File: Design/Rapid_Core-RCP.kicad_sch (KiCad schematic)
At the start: 1 part, among them U1 STM32F446RETx

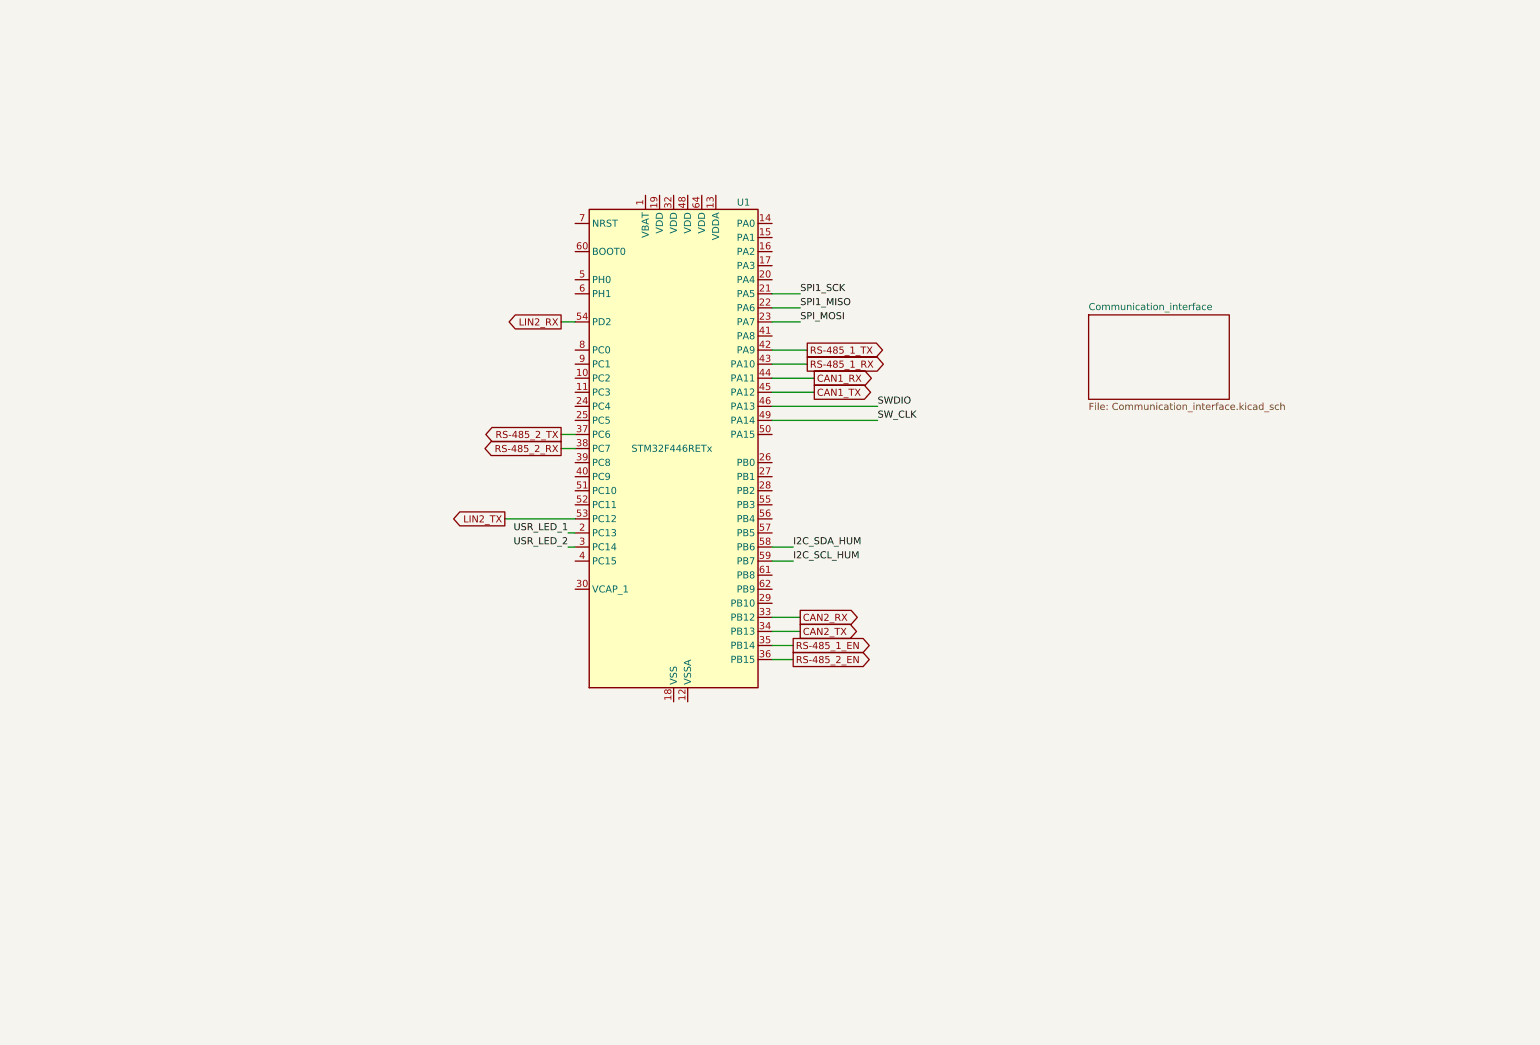
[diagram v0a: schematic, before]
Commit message: Added Comps in Communication.sch
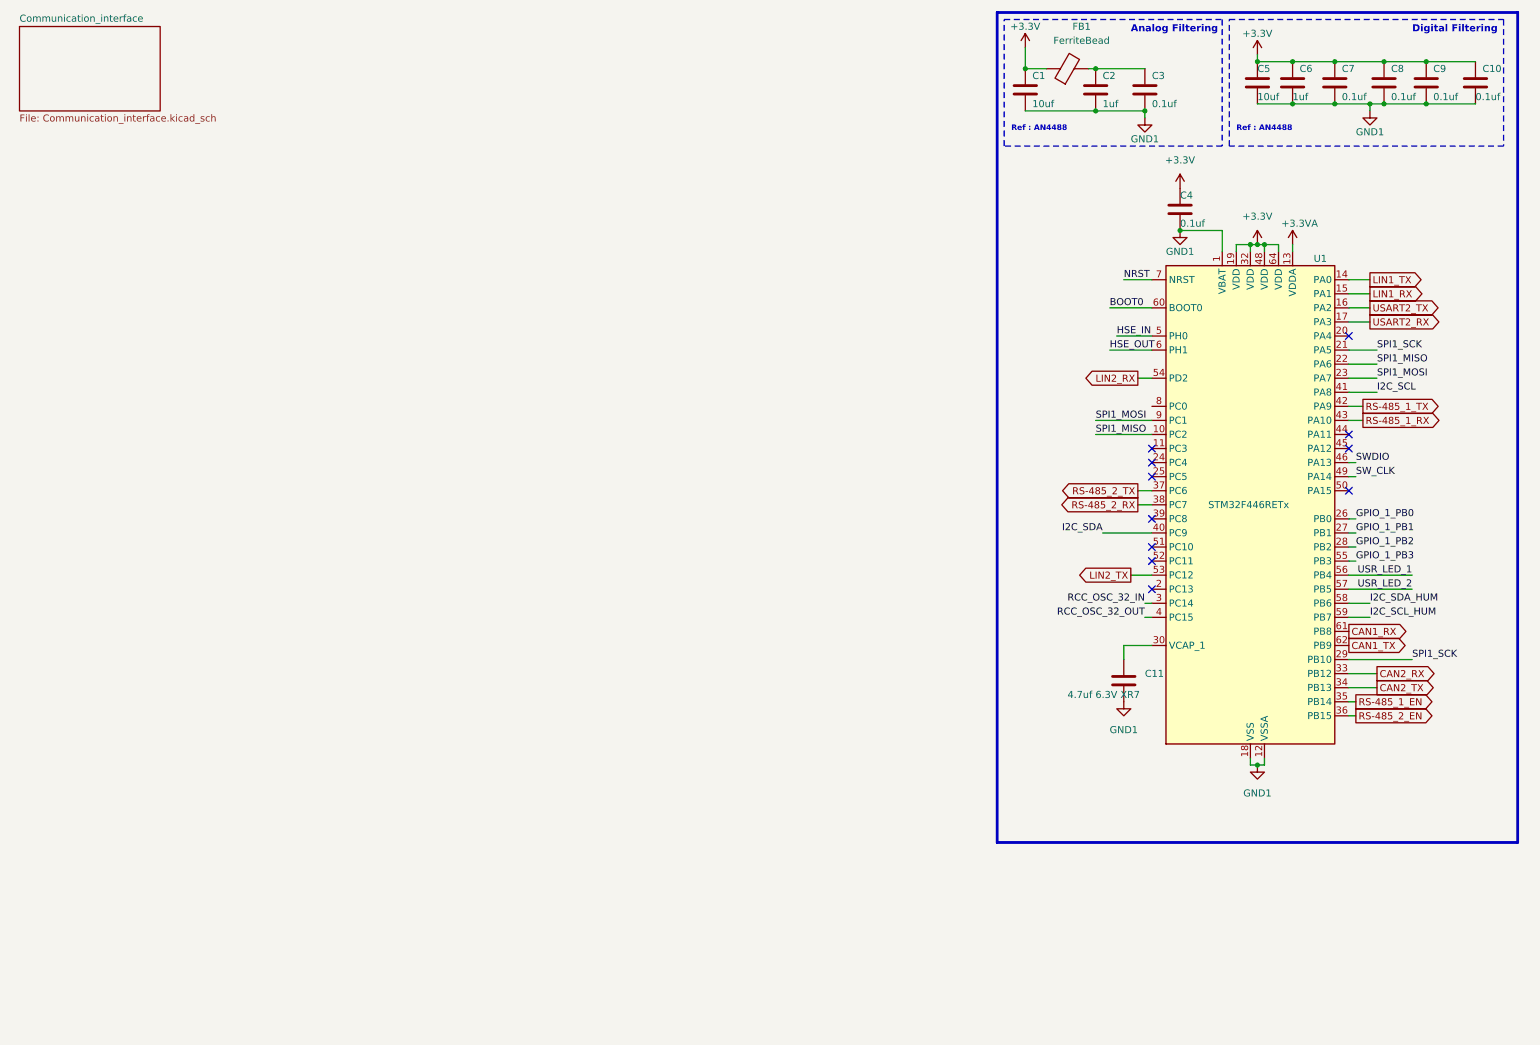
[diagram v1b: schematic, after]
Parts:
- added C1, C5: 10uf, symbol Device:C
- added C10, C3, C4, C7, C8, C9: 0.1uf, symbol Device:C
- added C11: 4.7uf 6.3V XR7, symbol Device:C
- added C2, C6: 1uf, symbol Device:C
- added FB1: FerriteBead, symbol Device:FerriteBead
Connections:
- net SPI_MOSI is gone; now on net SPI1_MOSI: U1.23 (PA7)
- net CAN1_RX: now also U1.61 (PB8); no longer U1.44 (PA11)
- net CAN1_TX: now also U1.62 (PB9); no longer U1.45 (PA12)
- net SPI1_MISO: now also U1.10 (PC2)
- net SPI1_SCK: now also U1.29 (PB10)
- net USR_LED_1: now also U1.56 (PB4); no longer U1.2 (PC13)
- net USR_LED_2: now also U1.57 (PB5); no longer U1.3 (PC14)
- net GND1: now reaches U1.1 (VBAT)
- net GND1: now also U1.12 (VSSA), U1.18 (VSS), U1.31 (VSS), U1.47 (VSS), U1.63 (VSS), C1.2, C10.2, C11.2, C2.2, C3.2, C4.2, C5.2, C6.2, C7.2, C8.2, C9.2
- net +3.3VA: now reaches U1.13 (VDDA)
- net LIN1_TX: now reaches U1.14 (PA0)
- net LIN1_RX: now reaches U1.15 (PA1)
- net USART2_TX: now reaches U1.16 (PA2)
- net USART2_RX: now reaches U1.17 (PA3)
- net +3.3V: now reaches U1.19 (VDD)
- net +3.3V: now also U1.32 (VDD), U1.48 (VDD), U1.64 (VDD), C1.1, C10.1, C4.1, C5.1, C6.1, C7.1, C8.1, C9.1, FB1.1
- net GPIO_1_PB0: now reaches U1.26 (PB0)
- net GPIO_1_PB1: now reaches U1.27 (PB1)
- net GPIO_1_PB2: now reaches U1.28 (PB2)
- net at U1.30 (VCAP_1): now also C11.1
- net RCC_OSC_32_OUT: now reaches U1.4 (PC15)
- net I2C_SDA: now reaches U1.40 (PC9)
- net I2C_SCL: now reaches U1.41 (PA8)
- net HSE_IN: now reaches U1.5 (PH0)
- net GPIO_1_PB3: now reaches U1.55 (PB3)
- net HSE_OUT: now reaches U1.6 (PH1)
- net BOOT0: now reaches U1.60 (BOOT0)
- net NRST: now reaches U1.7 (NRST)
- net SPI1_MOSI: now reaches U1.9 (PC1)
- new net: C2.1, C3.1, FB1.2
- new net RCC_OSC_32_IN: U1.3 (PC14)
- no-connect marks 0 -> 11
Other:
- note added: "Analog Filtering"
- note added: "Digital Filtering"
- note added: "Ref : AN4488"
- moved on the sheet: U1

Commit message: Added reference file for chokless CAN and DC-DC converter in main sch
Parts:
- added U6: CRE1S0505S3C, Converter_DCDC:Converter_DCDC_Murata_CRE1xxxxxx3C_THT, symbol Regulator_Switching:CRE1S0505S3C
- renumbered C9 to C10, C10 to C11, C11 to C3, C3 to C4, C4 to C5, C5 to C6, C6 to C7, C7 to C8, C8 to C9

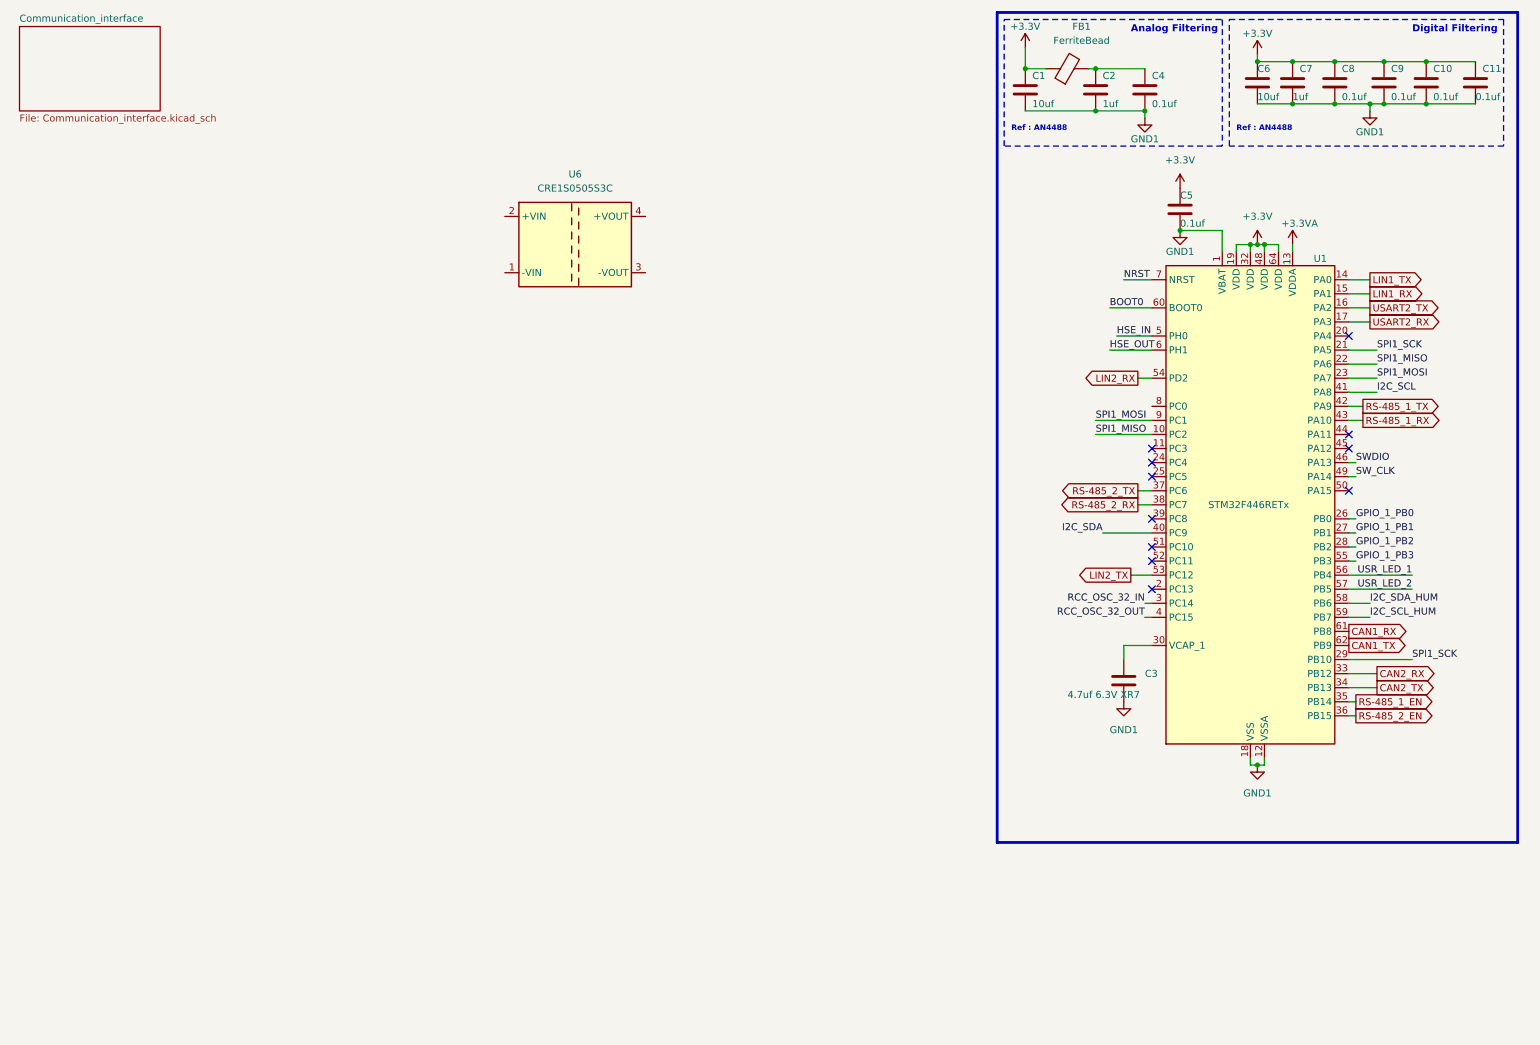
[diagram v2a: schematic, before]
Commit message: Communication.sch modified , 75% finished
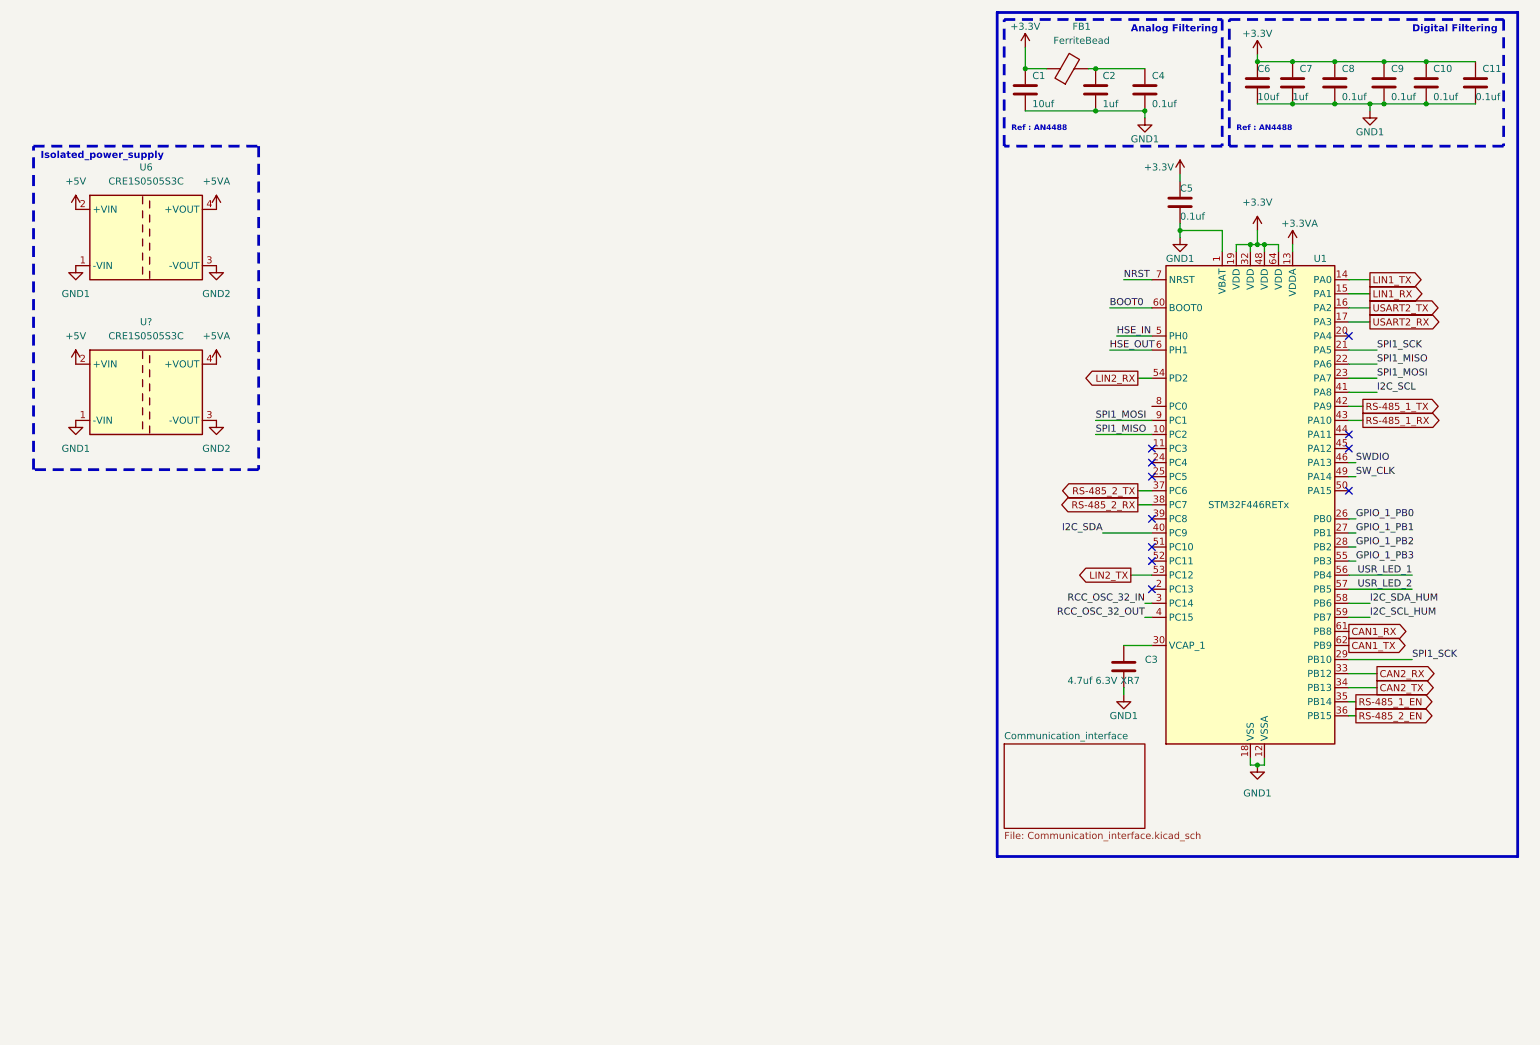
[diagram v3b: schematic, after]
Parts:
- added U?: CRE1S0505S3C, Converter_DCDC:Converter_DCDC_Murata_CRE1xxxxxx3C_THT, symbol Regulator_Switching:CRE1S0505S3C
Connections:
- net GND1: now also U6.1 (-VIN), U?.1 (-VIN)
- net +5V: now reaches U6.2 (+VIN)
- net +5V: now also U?.2 (+VIN)
- net GND2: now reaches U6.3 (-VOUT)
- net GND2: now also U?.3 (-VOUT)
- net +5VA: now reaches U6.4 (+VOUT)
- net +5VA: now also U?.4 (+VOUT)
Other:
- note added: "Isolated_power_supply"
- moved on the sheet: C3, C5, U6

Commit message: Added HUM and TEMP sense
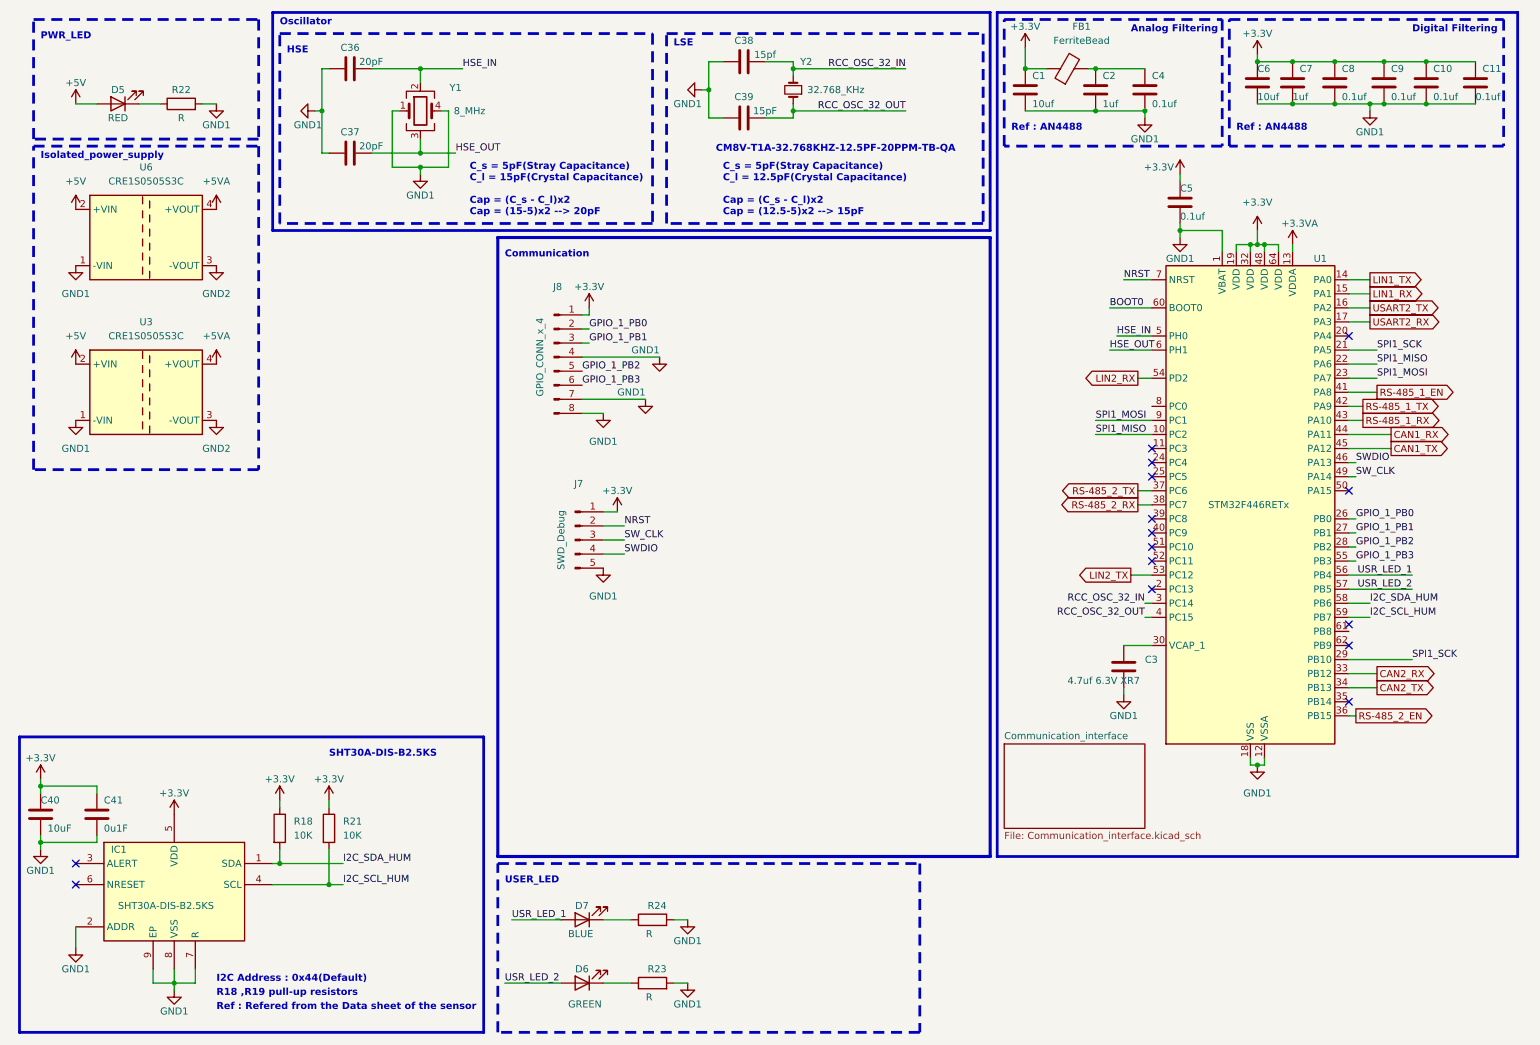
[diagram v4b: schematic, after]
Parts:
- added C36, C37: 20pF, symbol Device:C
- added C38: 15pf, symbol Device:C
- added C39: 15pF, symbol Device:C
- added C40: 10uF, symbol Device:C
- added C41: 0u1F, symbol Device:C
- added D5: RED, symbol Device:LED
- added D6: GREEN, symbol Device:LED
- added D7: BLUE, symbol Device:LED
- added IC1: SHT30A-DIS-B2.5KS, SHT30A-DIS-B2.5KS:SON50P250X250X100-9N-D, symbol SHT30A-DIS-B2_5KS:SHT30A-DIS-B2.5KS
- added J7: SWD_Debug, symbol Connector:Conn_01x05_Pin
- added J8: GPIO_CONN_x_4, symbol Connector:Conn_01x08_Pin
- added R18, R21: 10K, symbol Device:R
- added R22, R23, R24: R, symbol Device:R
- added Y1: 8_MHz, Crystal:Crystal_SMD_Abracon_ABM10-4Pin_2.5x2.0mm, symbol Device:Crystal_GND23
- added Y2: 32.768_KHz, Crystal:Crystal_SMD_MicroCrystal_CC8V-T1A-2Pin_2.0x1.2mm, symbol Device:Crystal_Small
- gave numbers to parts that had none: 1
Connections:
- net I2C_SCL is gone; now on net RS-485_1_EN: U1.41 (PA8)
- net +3.3V: now also C40.1, C41.1, IC1.5 (VDD), J7.1 (Pin_1), J8.1 (Pin_1), R18.1, R21.1
- net +5V: now also D5.2 (A)
- net CAN1_RX: now also U1.44 (PA11); no longer U1.61 (PB8)
- net CAN1_TX: now also U1.45 (PA12); no longer U1.62 (PB9)
- net GND1: now also C36.1, C37.1, C38.1, C39.1, C40.2, C41.2, IC1.2 (ADDR), IC1.7 (R), IC1.8 (VSS), IC1.9 (EP), J7.5 (Pin_5), J8.4 (Pin_4), J8.7 (Pin_7), J8.8 (Pin_8), R22.2, R23.2, R24.2, Y1.1, Y1.4
- net GPIO_1_PB0: now also J8.2 (Pin_2)
- net GPIO_1_PB1: now also J8.3 (Pin_3)
- net GPIO_1_PB2: now also J8.5 (Pin_5)
- net GPIO_1_PB3: now also J8.6 (Pin_6)
- net HSE_IN: now also C36.2, Y1.2
- net HSE_OUT: now also C37.2, Y1.3
- net I2C_SCL_HUM: now also IC1.4 (SCL), R21.2
- net I2C_SDA_HUM: now also IC1.1 (SDA), R18.2
- net NRST: now also J7.2 (Pin_2)
- net RCC_OSC_32_IN: now also C38.2, Y2.2
- net RCC_OSC_32_OUT: now also C39.2, Y2.1
- net RS-485_1_EN: no longer U1.35 (PB14)
- net SWDIO: now also J7.4 (Pin_4)
- net SW_CLK: now also J7.3 (Pin_3)
- net USR_LED_1: now also D7.2 (A)
- net USR_LED_2: now also D6.2 (A)
- net I2C_SDA: no longer names the net of U1.40 (PC9)
- new net: D7.1 (K), R24.1
- new net: D6.1 (K), R23.1
- new net: D5.1 (K), R22.1
- no-connect marks 11 -> 15
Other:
- note added: "CM8V-T1A-32.768KHZ-12.5PF-20PPM-TB-QA"
- note added: "C_s = 5pF(Stray Capacitance) C_l = 12.5pF(Crystal Capacitance) Cap = (C_s - C_l)x2 Cap = (12.5-5)x2 --> 15pF"
- note added: "C_s = 5pF(Stray Capacitance) C_l = 15pF(Crystal Capacitance) Cap = (C_s - C_l)x2 Cap = (15-5)x2 --> 20pF"
- note added: "Communication"
- note added: "HSE"
- note added: "I2C Address : 0x44(Default)"
- note added: "LSE"
- note added: "Oscillator"
- note added: "PWR_LED"
- note added: "R18 ,R19 pull-up resistors"
- note added: "Ref : Refered from the Data sheet of the sensor"
- note added: "SHT30A-DIS-B2.5KS"
- note added: "USER_LED"
